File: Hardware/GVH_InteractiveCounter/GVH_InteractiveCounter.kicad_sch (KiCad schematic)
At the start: 7 parts, among them J1 Molex Micro-Fit 5pos, J2 Molex Micro-Fit 5pos, U1 74HCT2G34GW_125, U2 SN74HC165N, U3 AT42QT1010, U4 74HC165

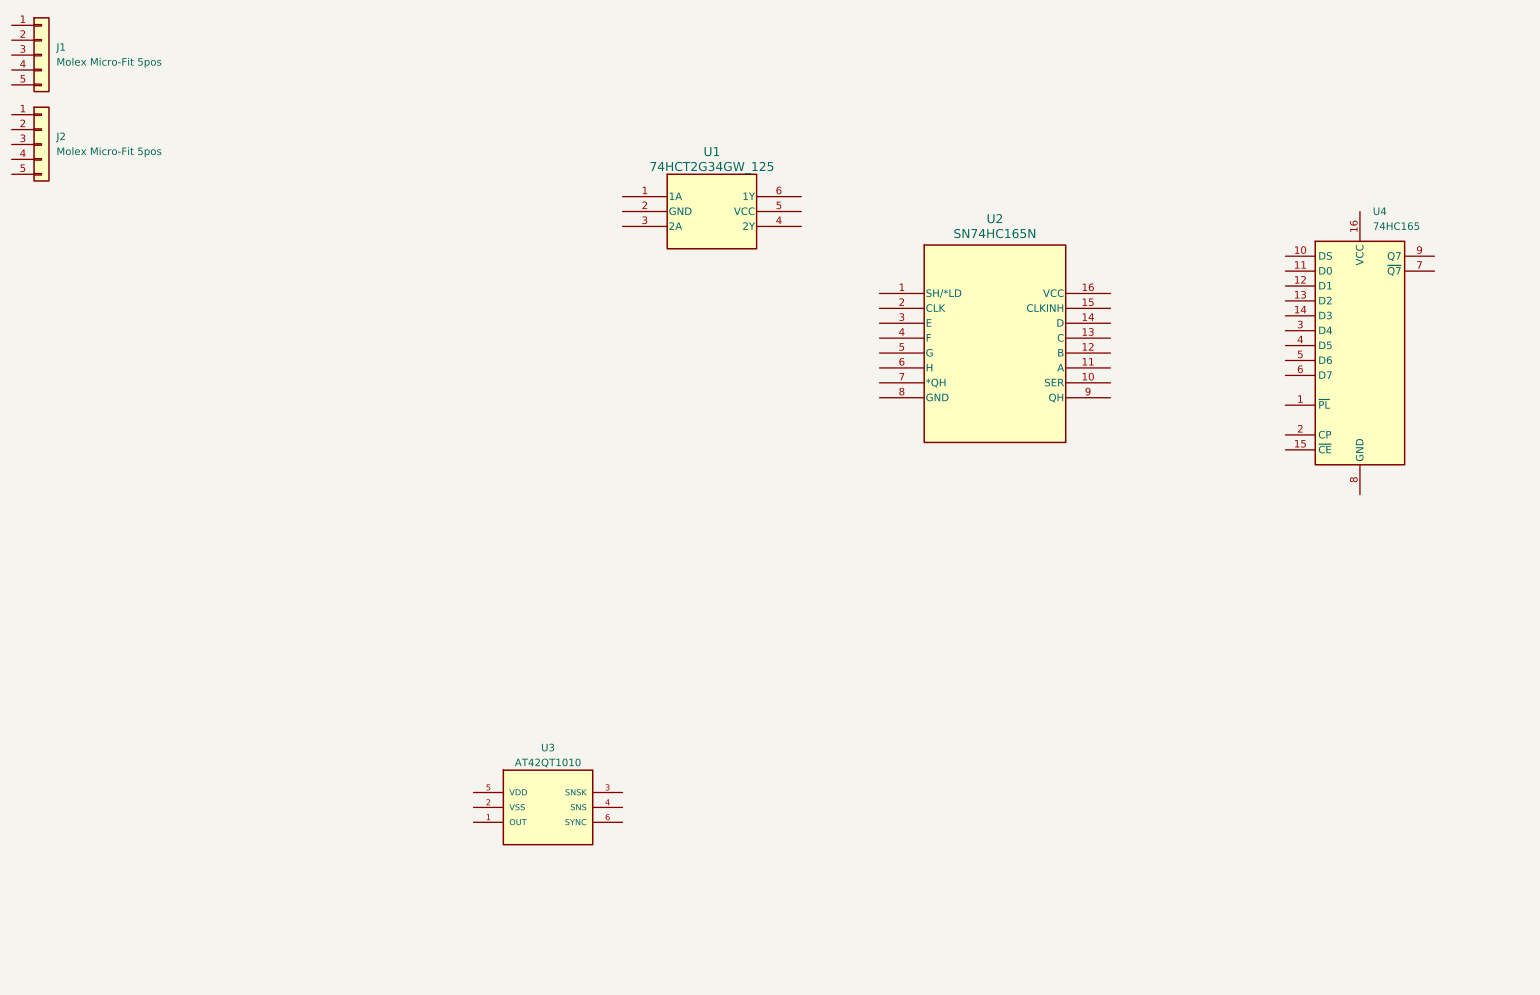
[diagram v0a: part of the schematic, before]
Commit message: Saving before changing from 1206 to 0805 components
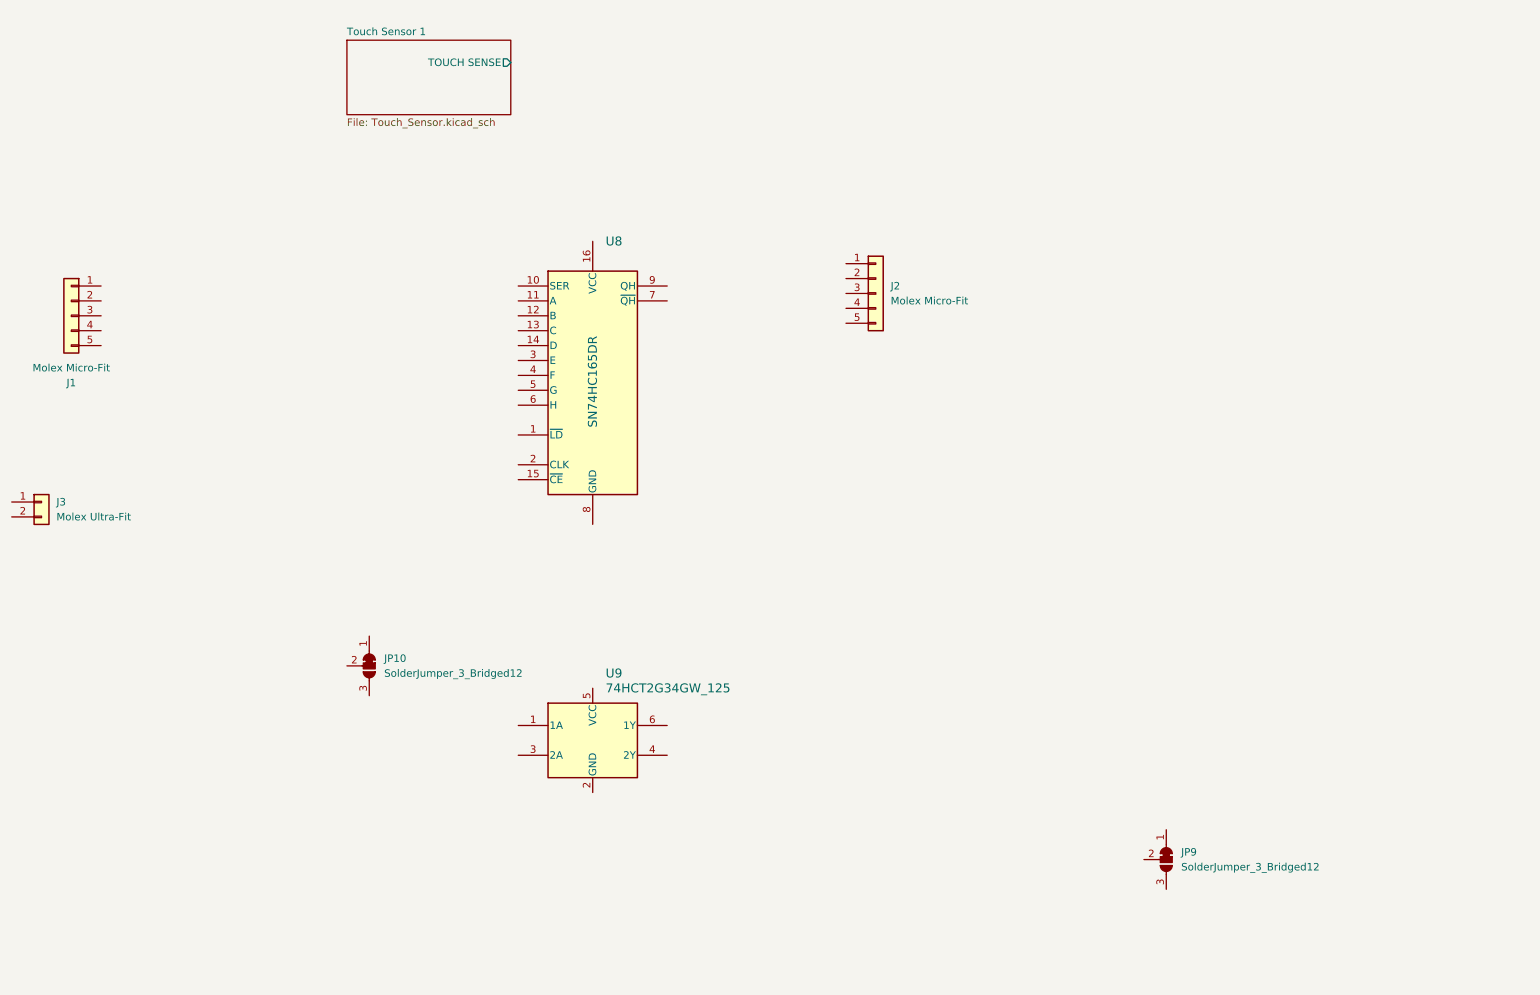
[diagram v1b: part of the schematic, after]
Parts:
- removed U1: 74HCT2G34GW_125, 0_integrated_circuits:SC-88_SOT363_NEX, symbol 0_integrated_circuits:74HCT2G34GW_125
- removed U2: SN74HC165N, Package_DIP:DIP-16_W10.16mm, symbol 0_integrated_circuits:SN74HC165N
- removed U3: AT42QT1010, 0_sensor:SOT95P270X145-6N, symbol 0_sensor:AT42QT1010-TSHR_1
- removed U4: 74HC165, symbol 74xx:74HC165
- added J3: Molex Ultra-Fit, 0_connector:MOLEX_ULTRAFIT-RA-2POS_1723104102, symbol 0_connector:Molex Ultra-Fit 2pos IN
- added JP10, JP9: SolderJumper_3_Bridged12, Jumper:SolderJumper-3_P1.3mm_Bridged12_RoundedPad1.0x1.5mm, symbol Jumper:SolderJumper_3_Bridged12
- added U8: SN74HC165DR, Package_SO:SOIC-16W_5.3x10.2mm_P1.27mm, symbol 0_integrated_circuits:SN74HC165N
- added U9: 74HCT2G34GW_125, 0_integrated_circuits:74HCT2G34GW_125_SOT363, symbol 0_integrated_circuits:74HCT2G34GW_125
- J1, J2: value Molex Micro-Fit 5pos -> Molex Micro-Fit
- LOGO1: now left out of the parts list
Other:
- added sheet Touch Sensor 1 (Touch_Sensor.kicad_sch)

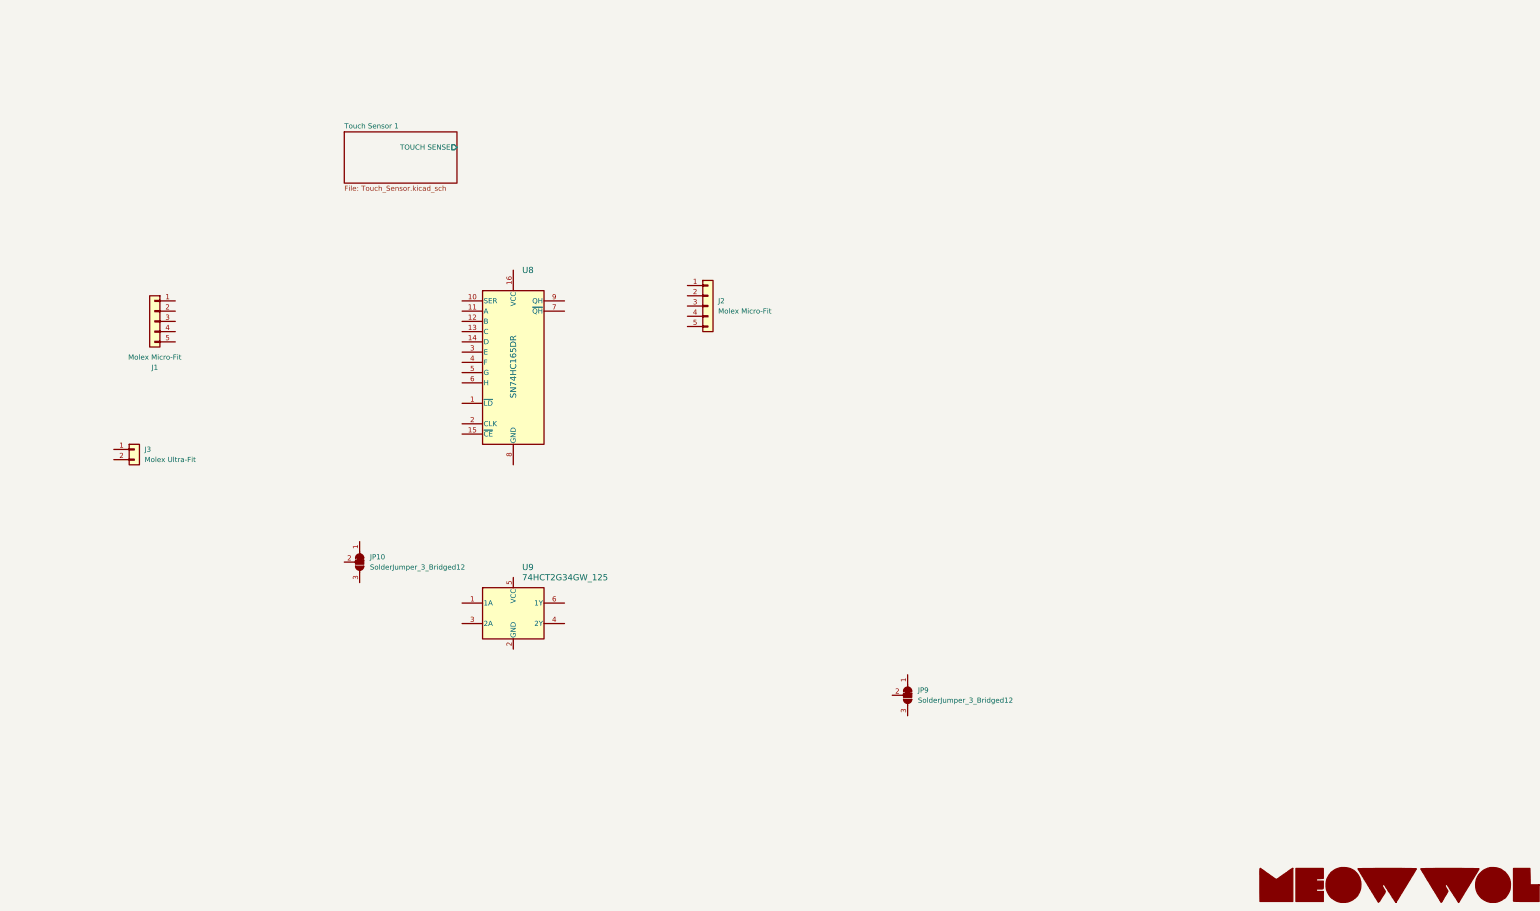
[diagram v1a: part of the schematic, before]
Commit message: Backing up work on PCB before some major changes
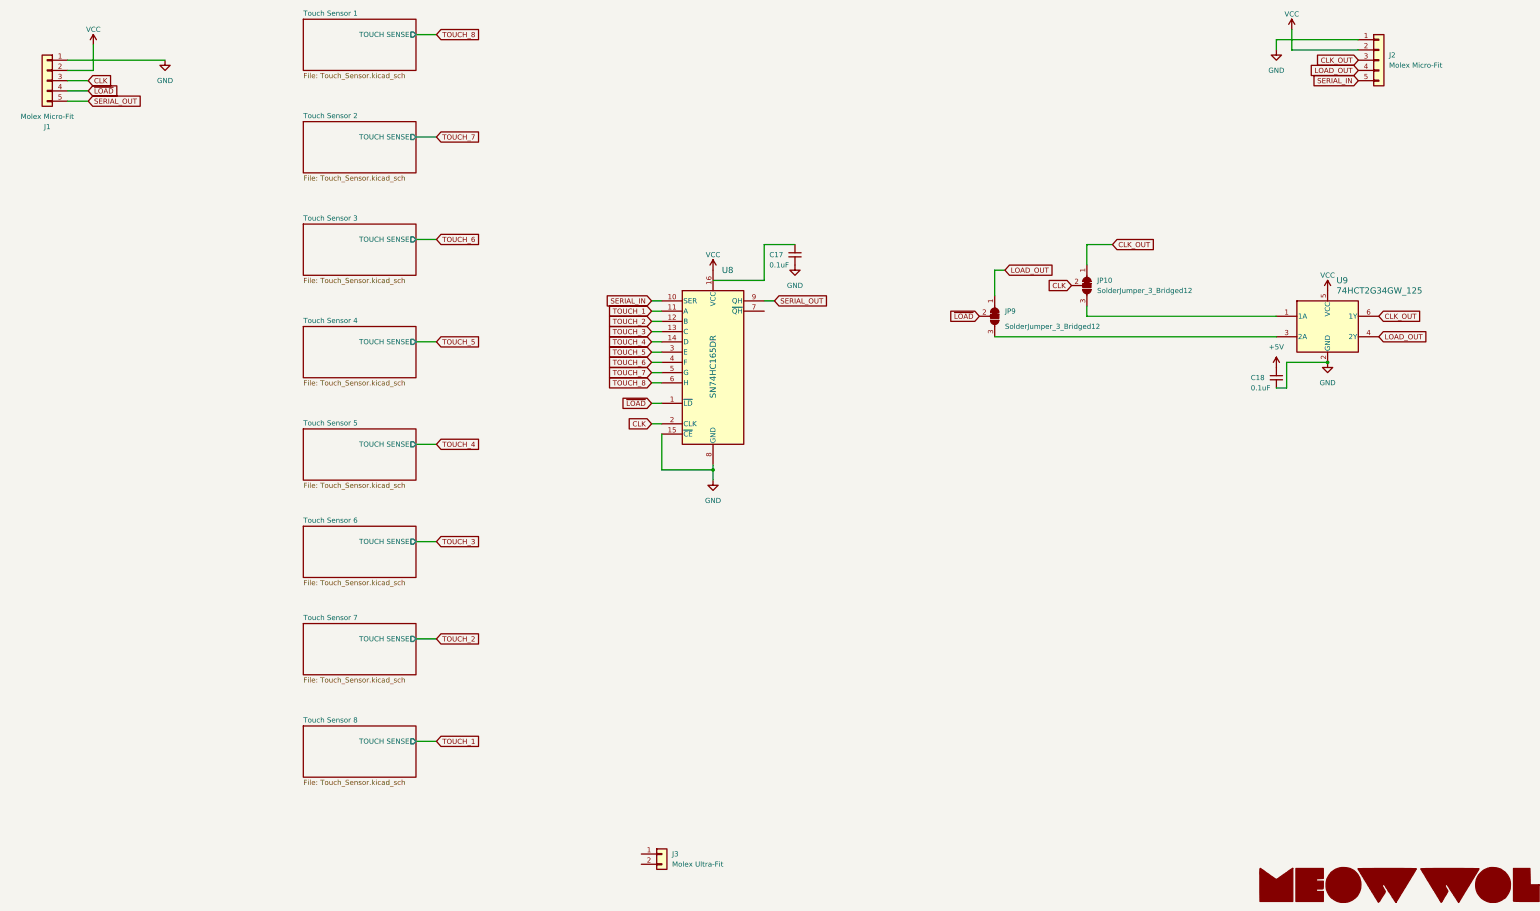
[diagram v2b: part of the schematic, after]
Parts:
- added C17, C18: 0.1uF, Capacitor_SMD:C_0805_2012Metric_Pad1.18x1.45mm_HandSolder, symbol Device:C_Small
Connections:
- net GND: now reaches J1.1 (Pin_1)
- net GND: now also J2.1 (Pin_1), U8.15 (~{CE}), U8.8 (GND), U9.2 (GND), C17.2, C18.2
- net VCC: now reaches J1.2 (Pin_2)
- net VCC: now also J2.2 (Pin_2), U8.16 (VCC), U9.5 (VCC)
- net CLK: now reaches J1.3 (Pin_3)
- net CLK: now also JP10.2 (C), U8.2 (CLK)
- net ~{LOAD}: now reaches J1.4 (Pin_4)
- net ~{LOAD}: now also JP9.2 (C), U8.1 (~{LD})
- net SERIAL_OUT: now reaches J1.5 (Pin_5)
- net SERIAL_OUT: now also U8.9 (QH)
- net LOAD_OUT: now reaches JP9.1 (A)
- net LOAD_OUT: now also J2.4 (Pin_4), U9.4 (2Y)
- net at JP9.3 (B): now also U9.3 (2A)
- net SERIAL_IN: now reaches U8.10 (SER)
- net SERIAL_IN: now also J2.5 (Pin_5)
- net TOUCH_1: now reaches U8.11 (A)
- net TOUCH_2: now reaches U8.12 (B)
- net TOUCH_3: now reaches U8.13 (C)
- net TOUCH_4: now reaches U8.14 (D)
- net TOUCH_5: now reaches U8.3 (E)
- net TOUCH_6: now reaches U8.4 (F)
- net TOUCH_7: now reaches U8.5 (G)
- net TOUCH_8: now reaches U8.6 (H)
- net CLK_OUT: now reaches JP10.1 (A)
- net CLK_OUT: now also J2.3 (Pin_3), U9.6 (1Y)
- net at JP10.3 (B): now also U9.1 (1A)
- new net +5V: C18.1
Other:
- added sheet Touch Sensor 2 (Touch_Sensor.kicad_sch)
- added sheet Touch Sensor 3 (Touch_Sensor.kicad_sch)
- added sheet Touch Sensor 4 (Touch_Sensor.kicad_sch)
- added sheet Touch Sensor 5 (Touch_Sensor.kicad_sch)
- added sheet Touch Sensor 6 (Touch_Sensor.kicad_sch)
- added sheet Touch Sensor 7 (Touch_Sensor.kicad_sch)
- added sheet Touch Sensor 8 (Touch_Sensor.kicad_sch)
- moved on the sheet: J1, J2, J3, JP10, JP9, U8, U9

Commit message: Board version 2 done. Not happy will start over
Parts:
- removed C18: 0.1uF, Capacitor_SMD:C_0805_2012Metric_Pad1.18x1.45mm_HandSolder, symbol Device:C_Small
- removed J3: Molex Ultra-Fit, 0_connector:MOLEX_ULTRAFIT-RA-2POS_1723104102, symbol 0_connector:Molex Ultra-Fit 2pos IN
- removed JP10, JP9: SolderJumper_3_Bridged12, Jumper:SolderJumper-3_P1.3mm_Bridged12_RoundedPad1.0x1.5mm, symbol Jumper:SolderJumper_3_Bridged12
- removed U9: 74HCT2G34GW_125, 0_integrated_circuits:74HCT2G34GW_125_SOT363, symbol 0_integrated_circuits:74HCT2G34GW_125
- added C19: 0.33uF, Capacitor_SMD:C_0805_2012Metric_Pad1.18x1.45mm_HandSolder, symbol Device:C_Small
- added C20, C22: 0.1uF, Capacitor_SMD:C_0805_2012Metric_Pad1.18x1.45mm_HandSolder, symbol Device:C_Small
- added J10, J11, J4, J5, J6, J7, J8, J9: Electrode, Connector_Pin:Pin_D1.3mm_L11.0mm_LooseFit, symbol Connector_Generic:Conn_01x01
- added J12, J13, J14, J15, J16, J17, J18, J19: Conn_01x01, Connector_PinHeader_2.54mm:PinHeader_1x01_P2.54mm_Vertical, symbol Connector_Generic:Conn_01x01
- added JP11, JP16, JP17: SolderJumper_2_Open, Jumper:SolderJumper-2_P1.3mm_Open_Pad1.0x1.5mm, symbol Jumper:SolderJumper_2_Open
- added JP14, JP15: SolderJumper_3_Bridged12, Jumper:SolderJumper-3_P1.3mm_Open_RoundedPad1.0x1.5mm_NumberLabels, symbol Jumper:SolderJumper_3_Open
- added R17, R18: 100, Resistor_SMD:R_0805_2012Metric_Pad1.20x1.40mm_HandSolder, symbol Device:R_Small
- added U11: L7805, Package_TO_SOT_THT:TO-220-3_Horizontal_TabDown, symbol Regulator_Linear:L7805
- added U13: SN74LVC2G17, Package_TO_SOT_SMD:SOT-23-6_Handsoldering, symbol 0_integrated_circuits:SN74LVC2G17
- J1, J2: footprint 0_connector:MOLEX_MICROFIT-RA-5POS_436500500 -> 0_connector:Molex_Micro-Fit_3.0_1x05_Horizontal_Vertical_Combo
- U8: footprint Package_SO:SOIC-16W_5.3x10.2mm_P1.27mm -> Package_SO:SOIC-16_3.9x9.9mm_P1.27mm
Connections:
- net +5V: now also C17.1, U8.16 (VCC), C20.1, C22.1, JP11.2 (B), U11.3 (OUT), U13.5 (VCC)
- net CLK: now also JP14.2 (C); no longer U8.2 (CLK)
- net CLK_OUT: now also U8.2 (CLK), JP16.2 (B), R17.1
- net GND: now also C19.2, C20.2, C22.2, J12.1 (Pin_1), J13.1 (Pin_1), J14.1 (Pin_1), J15.1 (Pin_1), J16.1 (Pin_1), J17.1 (Pin_1), J18.1 (Pin_1), J19.1 (Pin_1), U11.2 (GND), U13.2 (GND)
- net LOAD_OUT: now also U8.1 (~{LD}), JP17.2 (B), R18.1
- net TOUCH_1: now also U8.6 (H); no longer U8.11 (A)
- net TOUCH_2: now also U8.5 (G); no longer U8.12 (B)
- net TOUCH_3: now also U8.4 (F); no longer U8.13 (C)
- net TOUCH_4: now also U8.3 (E); no longer U8.14 (D)
- net TOUCH_5: now also U8.14 (D); no longer U8.3 (E)
- net TOUCH_6: now also U8.13 (C); no longer U8.4 (F)
- net TOUCH_7: now also U8.12 (B); no longer U8.5 (G)
- net TOUCH_8: now also U8.11 (A); no longer U8.6 (H)
- net VCC: now also C19.1, JP11.1 (A), U11.1 (IN); no longer U8.16 (VCC)
- net ~{LOAD}: now also JP15.2 (C); no longer U8.1 (~{LD})
- new net: JP14.1 (A), JP16.1 (A), R17.2, U13.6 (1Y)
- new net: JP15.1 (A), JP17.1 (A), R18.2, U13.4 (2Y)
- new net: JP14.3 (B), U13.1 (1A)
- new net: JP15.3 (B), U13.3 (2A)
- new net Touch Sensor 1/TOUCH_PAD: J4.1 (Pin_1)
- new net Touch Sensor 2/TOUCH_PAD: J5.1 (Pin_1)
- new net Touch Sensor 3/TOUCH_PAD: J6.1 (Pin_1)
- new net Touch Sensor 4/TOUCH_PAD: J7.1 (Pin_1)
- new net Touch Sensor 5/TOUCH_PAD: J8.1 (Pin_1)
- new net Touch Sensor 6/TOUCH_PAD: J9.1 (Pin_1)
- new net Touch Sensor 7/TOUCH_PAD: J10.1 (Pin_1)
- new net Touch Sensor 8/TOUCH_PAD: J11.1 (Pin_1)
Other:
- sheet Touch Sensor 1 ports: added TOUCH_PAD; removed none
- sheet Touch Sensor 2 ports: added TOUCH_PAD; removed none
- sheet Touch Sensor 3 ports: added TOUCH_PAD; removed none
- sheet Touch Sensor 4 ports: added TOUCH_PAD; removed none
- sheet Touch Sensor 5 ports: added TOUCH_PAD; removed none
- sheet Touch Sensor 6 ports: added TOUCH_PAD; removed none
- sheet Touch Sensor 7 ports: added TOUCH_PAD; removed none
- sheet Touch Sensor 8 ports: added TOUCH_PAD; removed none
- note added: "Buffers are optional for clock and load. Bridge solder pads to enable or bypass."
- moved on the sheet: C17, U8

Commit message: Finished another layout. This is probably the one.
Also  finished the touch pad layouts
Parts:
- J10, J11, J4, J5, J6, J7, J8, J9: footprint Connector_Pin:Pin_D1.3mm_L11.0mm_LooseFit -> Connector_Pin:Pin_D1.0mm_L10.0mm
- JP16, JP17: footprint Jumper:SolderJumper-2_P1.3mm_Open_Pad1.0x1.5mm -> Jumper:SolderJumper-2_P1.3mm_Open_RoundedPad1.0x1.5mm
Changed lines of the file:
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@@
       (effects (font (size 1.27 1.27)) hide)
     )
-    (property "Footprint" "Jumper:SolderJumper-2_P1.3mm_Open_Pad1.0x1.5mm" (at 114.3 151.13 0)
+    (property "Footprint" "Jumper:SolderJumper-2_P1.3mm_Open_RoundedPad1.0x1.5mm" (at 114.3 151.13 0)
       (effects (font (size 1.27 1.27)) hide)
     )
@@
       (effects (font (size 1.27 1.27)) (justify left))
     )
-    (property "Footprint" "Connector_Pin:Pin_D1.3mm_L11.0mm_LooseFit" (at 204.47 134.62 0)
+    (property "Footprint" "Connector_Pin:Pin_D1.0mm_L10.0mm" (at 204.47 134.62 0)
       (effects (font (size 1.27 1.27)) hide)
     )
@@
       (effects (font (size 1.27 1.27)) (justify left))
     )
-    (property "Footprint" "Connector_Pin:Pin_D1.3mm_L11.0mm_LooseFit" (at 204.47 158.75 0)
+    (property "Footprint" "Connector_Pin:Pin_D1.0mm_L10.0mm" (at 204.47 158.75 0)
       (effects (font (size 1.27 1.27)) hide)
     )
@@
       (effects (font (size 1.27 1.27)) (justify left))
     )
-    (property "Footprint" "Connector_Pin:Pin_D1.3mm_L11.0mm_LooseFit" (at 204.47 109.22 0)
+    (property "Footprint" "Connector_Pin:Pin_D1.0mm_L10.0mm" (at 204.47 109.22 0)
       (effects (font (size 1.27 1.27)) hide)
     )
@@
       (effects (font (size 1.27 1.27)) (justify left))
     )
-    (property "Footprint" "Connector_Pin:Pin_D1.3mm_L11.0mm_LooseFit" (at 204.47 208.28 0)
+    (property "Footprint" "Connector_Pin:Pin_D1.0mm_L10.0mm" (at 204.47 208.28 0)
       (effects (font (size 1.27 1.27)) hide)
     )
@@
       (effects (font (size 1.27 1.27)) hide)
     )
-    (property "Footprint" "Jumper:SolderJumper-2_P1.3mm_Open_Pad1.0x1.5mm" (at 114.3 166.37 0)
+    (property "Footprint" "Jumper:SolderJumper-2_P1.3mm_Open_RoundedPad1.0x1.5mm" (at 114.3 166.37 0)
       (effects (font (size 1.27 1.27)) hide)
     )
@@
       (effects (font (size 1.27 1.27)) (justify left))
     )
-    (property "Footprint" "Connector_Pin:Pin_D1.3mm_L11.0mm_LooseFit" (at 204.47 33.02 0)
+    (property "Footprint" "Connector_Pin:Pin_D1.0mm_L10.0mm" (at 204.47 33.02 0)
       (effects (font (size 1.27 1.27)) hide)
     )
@@
       (effects (font (size 1.27 1.27)) (justify left))
     )
-    (property "Footprint" "Connector_Pin:Pin_D1.3mm_L11.0mm_LooseFit" (at 204.47 83.82 0)
+    (property "Footprint" "Connector_Pin:Pin_D1.0mm_L10.0mm" (at 204.47 83.82 0)
       (effects (font (size 1.27 1.27)) hide)
     )
@@
       (effects (font (size 1.27 1.27)) (justify left))
     )
-    (property "Footprint" "Connector_Pin:Pin_D1.3mm_L11.0mm_LooseFit" (at 204.47 58.42 0)
+    (property "Footprint" "Connector_Pin:Pin_D1.0mm_L10.0mm" (at 204.47 58.42 0)
       (effects (font (size 1.27 1.27)) hide)
     )
@@
       (effects (font (size 1.27 1.27)) (justify left))
     )
-    (property "Footprint" "Connector_Pin:Pin_D1.3mm_L11.0mm_LooseFit" (at 204.47 182.88 0)
-      (effects (font (size 1.27 1.27)) hide)
-    )
+    (property "Footprint" "Connector_Pin:Pin_D1.0mm_L10.0mm" (at 204.47 182.88 0)
+      (effects (font (size 1.27 1.27)) hide)
+    )
